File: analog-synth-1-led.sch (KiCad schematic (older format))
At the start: 6 parts

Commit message: Annotate components
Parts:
- gave numbers to parts that had none: 6
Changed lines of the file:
@@
 $EndDescr
 $Comp
-L MCU_Microchip_ATtiny:ATtiny85-20PU U?
+L MCU_Microchip_ATtiny:ATtiny85-20PU U3
 U 1 1 5C8BBB94
 P 5650 3750
-F 0 "U?" H 5120 3796 50  0000 R CNN
+F 0 "U3" H 5120 3796 50  0000 R CNN
 F 1 "ATtiny85-20PU" H 5120 3705 50  0000 R CNN
 F 2 "Package_DIP:DIP-8_W7.62mm" H 5650 3750 50  0001 C CIN
@@
 $EndComp
 $Comp
-L power:+5V #PWR?
+L power:+5V #PWR031
 U 1 1 5C8BBC25
 P 5650 3050
-F 0 "#PWR?" H 5650 2900 50  0001 C CNN
+F 0 "#PWR031" H 5650 2900 50  0001 C CNN
 F 1 "+5V" H 5665 3223 50  0000 C CNN
 F 2 "" H 5650 3050 50  0001 C CNN
@@
 	5650 3050 5650 3100
 $Comp
-L power:GND #PWR?
+L power:GND #PWR032
 U 1 1 5C8BBC54
 P 5650 4450
-F 0 "#PWR?" H 5650 4200 50  0001 C CNN
+F 0 "#PWR032" H 5650 4200 50  0001 C CNN
 F 1 "GND" H 5655 4277 50  0000 C CNN
 F 2 "" H 5650 4450 50  0001 C CNN
@@
 	5650 3100 5650 3150
 $Comp
-L Device:LED_RAGB D?
+L Device:LED_RAGB D1
 U 1 1 5C8BC0D1
 P 7350 3650
-F 0 "D?" H 7350 4147 50  0000 C CNN
+F 0 "D1" H 7350 4147 50  0000 C CNN
 F 1 "LED_RAGB" H 7350 4056 50  0000 C CNN
 F 2 "" H 7350 3600 50  0001 C CNN
@@
 	7050 3650 7050 3550
 $Comp
-L Device:R R?
+L Device:R R21
 U 1 1 5C8BC2EB
 P 6900 3450
-F 0 "R?" V 6693 3450 50  0000 C CNN
+F 0 "R21" V 6693 3450 50  0000 C CNN
 F 1 "180" V 6784 3450 50  0000 C CNN
 F 2 "" V 6830 3450 50  0001 C CNN
@@
 $EndComp
 $Comp
-L Device:R R?
+L Device:R R20
 U 1 1 5C8BC33C
 P 6600 3550
-F 0 "R?" V 6393 3550 50  0000 C CNN
+F 0 "R20" V 6393 3550 50  0000 C CNN
 F 1 "150" V 6484 3550 50  0000 C CNN
 F 2 "" V 6530 3550 50  0001 C CNN
@@
 $EndComp
 $Comp
-L Device:R R?
+L Device:R R22
 U 1 1 5C8BC383
 P 6900 3850
-F 0 "R?" V 6693 3850 50  0000 C CNN
+F 0 "R22" V 6693 3850 50  0000 C CNN
 F 1 "130" V 6784 3850 50  0000 C CNN
 F 2 "" V 6830 3850 50  0001 C CNN
@@
 	7150 3850 7050 3850
 $Comp
-L power:+5V #PWR?
+L power:+5V #PWR033
 U 1 1 5C8BCB00
 P 7700 3500
-F 0 "#PWR?" H 7700 3350 50  0001 C CNN
+F 0 "#PWR033" H 7700 3350 50  0001 C CNN
 F 1 "+5V" H 7715 3673 50  0000 C CNN
 F 2 "" H 7700 3500 50  0001 C CNN
@@
 	5650 4400 5650 4350
 $Comp
-L Device:C C?
+L Device:C C9
 U 1 1 5C8C58CD
 P 3850 3750
-F 0 "C?" H 3965 3796 50  0000 L CNN
+F 0 "C9" H 3965 3796 50  0000 L CNN
 F 1 "100nf" H 3965 3705 50  0000 L CNN
 F 2 "" H 3888 3600 50  0001 C CNN

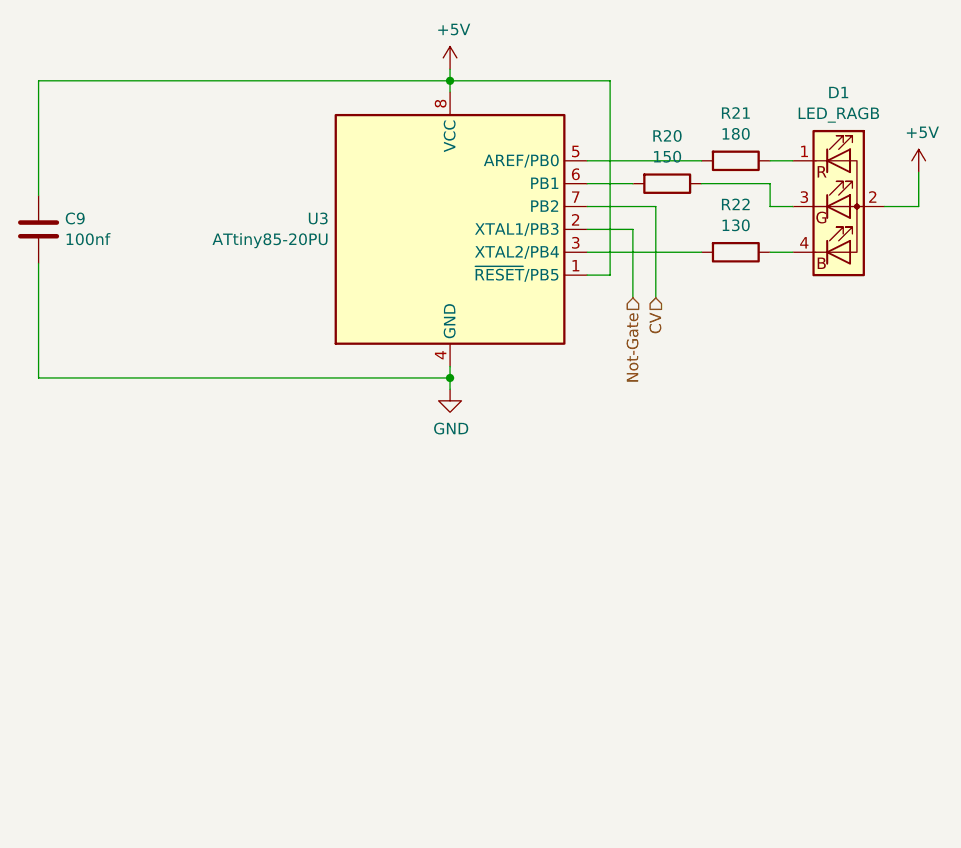
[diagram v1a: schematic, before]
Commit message: Add ATtiny85 overdrive protection, fix #5
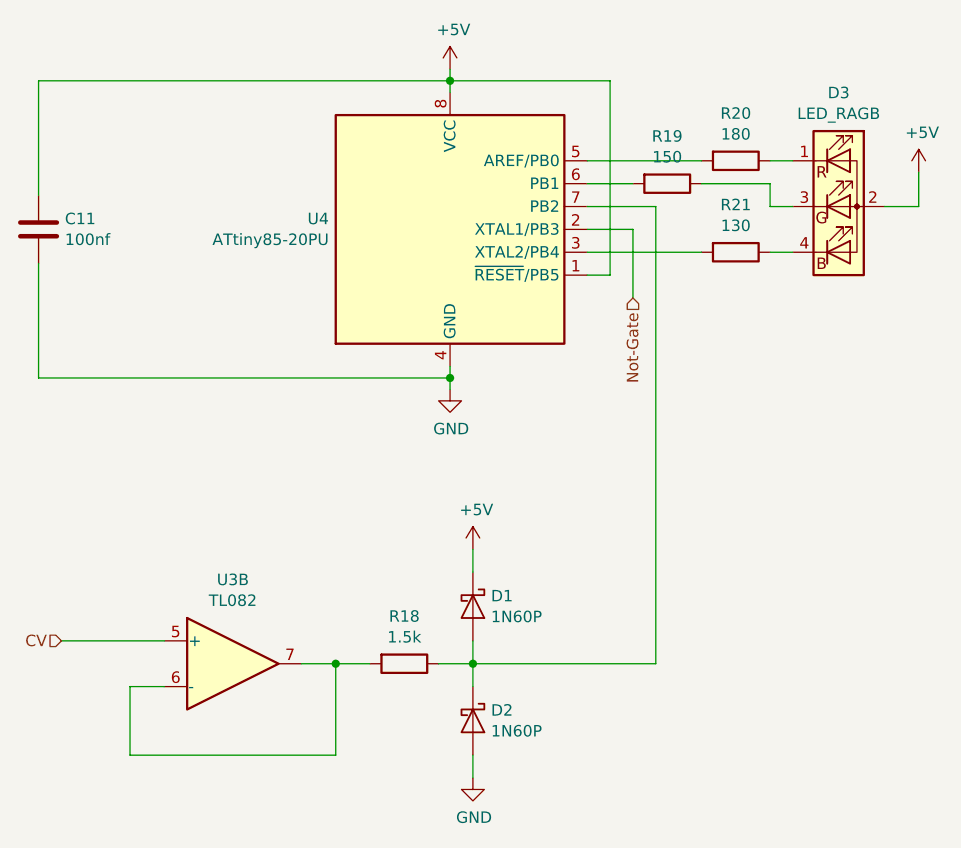
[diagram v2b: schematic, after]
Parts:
- added D1, D2: 1N60P, symbol Device:D_Schottky
- added R18: 1.5k, symbol Device:R
- added U3: TL082, symbol Amplifier_Operational:TL082
- renumbered C9 to C11, D1 to D3, R20 to R19, R21 to R20, R22 to R21, U3 to U4
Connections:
- net +5V: now also D1.1 (K)
- net CV: now also U3.5 (+); no longer U4.7 (PB2)
- net GND: now also D2.2 (A)
- new net: D1.2 (A), D2.1 (K), R18.1, U4.7 (PB2)
- new net: R18.2, U3.6 (-), U3.7
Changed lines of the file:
@@
 $EndDescr
 $Comp
-L MCU_Microchip_ATtiny:ATtiny85-20PU U3
+L MCU_Microchip_ATtiny:ATtiny85-20PU U4
 U 1 1 5C8BBB94
 P 5650 3750
-F 0 "U3" H 5120 3796 50  0000 R CNN
+F 0 "U4" H 5120 3796 50  0000 R CNN
 F 1 "ATtiny85-20PU" H 5120 3705 50  0000 R CNN
 F 2 "Package_DIP:DIP-8_W7.62mm" H 5650 3750 50  0001 C CIN
@@
 $EndComp
 $Comp
-L power:+5V #PWR031
+L power:+5V #PWR034
 U 1 1 5C8BBC25
 P 5650 3050
-F 0 "#PWR031" H 5650 2900 50  0001 C CNN
+F 0 "#PWR034" H 5650 2900 50  0001 C CNN
 F 1 "+5V" H 5665 3223 50  0000 C CNN
 F 2 "" H 5650 3050 50  0001 C CNN
@@
 	5650 3050 5650 3100
 $Comp
-L power:GND #PWR032
+L power:GND #PWR035
 U 1 1 5C8BBC54
 P 5650 4450
-F 0 "#PWR032" H 5650 4200 50  0001 C CNN
+F 0 "#PWR035" H 5650 4200 50  0001 C CNN
 F 1 "GND" H 5655 4277 50  0000 C CNN
 F 2 "" H 5650 4450 50  0001 C CNN
@@
 	5650 3100 5650 3150
 $Comp
-L Device:LED_RAGB D1
+L Device:LED_RAGB D3
 U 1 1 5C8BC0D1
 P 7350 3650
-F 0 "D1" H 7350 4147 50  0000 C CNN
+F 0 "D3" H 7350 4147 50  0000 C CNN
 F 1 "LED_RAGB" H 7350 4056 50  0000 C CNN
 F 2 "" H 7350 3600 50  0001 C CNN
@@
 	7050 3650 7050 3550
 $Comp
-L Device:R R21
+L Device:R R20
 U 1 1 5C8BC2EB
 P 6900 3450
-F 0 "R21" V 6693 3450 50  0000 C CNN
+F 0 "R20" V 6693 3450 50  0000 C CNN
 F 1 "180" V 6784 3450 50  0000 C CNN
 F 2 "" V 6830 3450 50  0001 C CNN
@@
 $EndComp
 $Comp
-L Device:R R20
+L Device:R R19
 U 1 1 5C8BC33C
 P 6600 3550
-F 0 "R20" V 6393 3550 50  0000 C CNN
+F 0 "R19" V 6393 3550 50  0000 C CNN
 F 1 "150" V 6484 3550 50  0000 C CNN
 F 2 "" V 6530 3550 50  0001 C CNN
@@
 $EndComp
 $Comp
-L Device:R R22
+L Device:R R21
 U 1 1 5C8BC383
 P 6900 3850
-F 0 "R22" V 6693 3850 50  0000 C CNN
+F 0 "R21" V 6693 3850 50  0000 C CNN
 F 1 "130" V 6784 3850 50  0000 C CNN
 F 2 "" V 6830 3850 50  0001 C CNN
@@
 	7150 3850 7050 3850
 $Comp
-L power:+5V #PWR033
+L power:+5V #PWR038
 U 1 1 5C8BCB00
 P 7700 3500
-F 0 "#PWR033" H 7700 3350 50  0001 C CNN
+F 0 "#PWR038" H 7700 3350 50  0001 C CNN
 F 1 "+5V" H 7715 3673 50  0000 C CNN
 F 2 "" H 7700 3500 50  0001 C CNN
@@
 Wire Wire Line
 	7700 3650 7550 3650
-Text HLabel 6550 4050 3    50   Input ~ 0
+Text HLabel 3950 5550 0    50   Input ~ 0
 CV
 Text HLabel 6450 4050 3    50   Input ~ 0
@@
 	6450 3750 6250 3750
 Wire Wire Line
-	6550 4050 6550 3650
-Wire Wire Line
 	6550 3650 6250 3650
 Wire Wire Line
@@
 	5650 4400 5650 4350
 $Comp
-L Device:C C9
+L Device:C C11
 U 1 1 5C8C58CD
 P 3850 3750
-F 0 "C9" H 3965 3796 50  0000 L CNN
+F 0 "C11" H 3965 3796 50  0000 L CNN
 F 1 "100nf" H 3965 3705 50  0000 L CNN
 F 2 "" H 3888 3600 50  0001 C CNN
@@
 	1    0    0    -1
 $EndComp
+$Comp
+L Amplifier_Operational:TL082 U3
+U 2 1 5CA1B8BF
+P 4700 5650
+F 0 "U3" H 4700 6017 50  0000 C CNN
+F 1 "TL082" H 4700 5926 50  0000 C CNN
+F 2 "" H 4700 5650 50  0001 C CNN
+F 3 "http://www.ti.com/lit/ds/symlink/tl081.pdf" H 4700 5650 50  0001 C CNN
+	2    4700 5650
+	1    0    0    -1
+$EndComp
+Wire Wire Line
+	3950 5550 4400 5550
+Wire Wire Line
+	4400 5750 4250 5750
+Wire Wire Line
+	4250 5750 4250 6050
+Wire Wire Line
+	4250 6050 5150 6050
+Wire Wire Line
+	5150 6050 5150 5650
+Wire Wire Line
+	5150 5650 5000 5650
+$Comp
+L Device:R R18
+U 1 1 5CA1C430
+P 5450 5650
+F 0 "R18" V 5243 5650 50  0000 C CNN
+F 1 "1.5k" V 5334 5650 50  0000 C CNN
+F 2 "" V 5380 5650 50  0001 C CNN
+F 3 "~" H 5450 5650 50  0001 C CNN
+	1    5450 5650
+	0    1    1    0
+$EndComp
+Wire Wire Line
+	5300 5650 5150 5650
+Connection ~ 5150 5650
+$Comp
+L Device:D_Schottky D2
+U 1 1 5CA1CA36
+P 5750 5900
+F 0 "D2" V 5704 5979 50  0000 L CNN
+F 1 "1N60P" V 5795 5979 50  0000 L CNN
+F 2 "" H 5750 5900 50  0001 C CNN
+F 3 "~" H 5750 5900 50  0001 C CNN
+	1    5750 5900
+	0    1    1    0
+$EndComp
+$Comp
+L Device:D_Schottky D1
+U 1 1 5CA1CADF
+P 5750 5400
+F 0 "D1" V 5704 5479 50  0000 L CNN
+F 1 "1N60P" V 5795 5479 50  0000 L CNN
+F 2 "" H 5750 5400 50  0001 C CNN
+F 3 "~" H 5750 5400 50  0001 C CNN
+	1    5750 5400
+	0    1    1    0
+$EndComp
+Wire Wire Line
+	5600 5650 5750 5650
+Wire Wire Line
+	5750 5650 5750 5550
+Wire Wire Line
+	5750 5650 5750 5750
+Connection ~ 5750 5650
+$Comp
+L power:+5V #PWR036
+U 1 1 5CA1D6EB
+P 5750 5150
+F 0 "#PWR036" H 5750 5000 50  0001 C CNN
+F 1 "+5V" H 5765 5323 50  0000 C CNN
+F 2 "" H 5750 5150 50  0001 C CNN
+F 3 "" H 5750 5150 50  0001 C CNN
+	1    5750 5150
+	1    0    0    -1
+$EndComp
+Wire Wire Line
+	5750 5150 5750 5250
+$Comp
+L power:GND #PWR037
+U 1 1 5CA1DD7E
+P 5750 6150
+F 0 "#PWR037" H 5750 5900 50  0001 C CNN
+F 1 "GND" H 5755 5977 50  0000 C CNN
+F 2 "" H 5750 6150 50  0001 C CNN
+F 3 "" H 5750 6150 50  0001 C CNN
+	1    5750 6150
+	1    0    0    -1
+$EndComp
+Wire Wire Line
+	5750 6150 5750 6050
+Wire Wire Line
+	5750 5650 6550 5650
+Wire Wire Line
+	6550 3650 6550 5650
 $EndSCHEMATC
